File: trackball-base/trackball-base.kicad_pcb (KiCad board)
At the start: 2 copper layers, 110 x 140 mm, 159 parts, among them J201 TYPE-C-31-M-12, J202 CORTEX-DBG-10, Q101 2N7002, SW201 RESET, SW202 BOOT, SW401 D2FC-F-7N, SW402 D2FC-F-7N, SW403 D2FC-F-7N, U101 AP2112K-3.3TRG1, U102 APX809-29SAG-7, U103 XC6206P192MR, U104 TPS22918DBVR, U105 TPS22918DBVR, U106 TLV3011AIDBVR, U107 TLV3011AIDBVR, U201 E73-2G4M08S1C, U202 TPD2E1B06DRLR, U301 PMW3360DM-T2QU, U302 PMW3360DM-T2QU, U501 LTC4125EUFD, Y201 ABS07-32.768KHZ-9-T

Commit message: Q6 WaveC: J202-Pin2 closed (B-route + VSEN-via bypass + pad via); drc168 16unc/0err/0parity
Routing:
- net /mcu/Net-(J202-Pin_2): track 24.2 -> 43.3 mm, vias 2 -> 4
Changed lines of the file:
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@@
+	)
+	(via
+		(at 12.2 9.45)
+		(size 0.6)
+		(drill 0.3)
+		(layers "F.Cu" "B.Cu")
+		(net "/mcu/Net-(J202-Pin_2)")
+	)
+	(via
+		(at 9.95 19.7)
+		(size 0.6)
+		(drill 0.3)
+		(layers "F.Cu" "B.Cu")
+		(net "/mcu/Net-(J202-Pin_2)")
 	)
 	(via
@@
 		(drill 0.4)
 		(layers "F.Cu" "B.Cu")
+		(net "/mcu/Net-(J202-Pin_2)")
+	)
+	(segment
+		(start 13.8 9.45)
+		(end 13.8 16.85)
+		(width 0.25)
+		(layer "B.Cu")
+		(net "/mcu/Net-(J202-Pin_2)")
+	)
+	(segment
+		(start 9.95 19.46)
+		(end 9.95 20.5)
+		(width 0.25)
+		(layer "B.Cu")
+		(net "/mcu/Net-(J202-Pin_2)")
+	)
+	(segment
+		(start 9.95 20.5)
+		(end 13.8 20.5)
+		(width 0.25)
+		(layer "B.Cu")
+		(net "/mcu/Net-(J202-Pin_2)")
+	)
+	(segment
+		(start 13 18.15)
+		(end 13.8 18.15)
+		(width 0.25)
+		(layer "B.Cu")
+		(net "/mcu/Net-(J202-Pin_2)")
+	)
+	(segment
+		(start 13 16.85)
+		(end 13 18.15)
+		(width 0.25)
+		(layer "B.Cu")
 		(net "/mcu/Net-(J202-Pin_2)")
 	)
@@
 	)
 	(segment
+		(start 13.8 16.85)
+		(end 13 16.85)
+		(width 0.25)
+		(layer "B.Cu")
+		(net "/mcu/Net-(J202-Pin_2)")
+	)
+	(segment
 		(start 29.925 8.81)
 		(end 25.703 8.81)
 		(width 0.25)
 		(layer "B.Cu")
+		(net "/mcu/Net-(J202-Pin_2)")
+	)
+	(segment
+		(start 13.8 9.45)
+		(end 12.2 9.45)
+		(width 0.25)
+		(layer "B.Cu")
+		(net "/mcu/Net-(J202-Pin_2)")
+	)
+	(segment
+		(start 13.8 18.15)
+		(end 13.8 20.5)
+		(width 0.25)
+		(layer "B.Cu")

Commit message: Q6 WaveC complete: FTH ripped; drc177 16unc/0err/0parity; WaveD=15+WaveZ
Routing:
- net S2_MOT: track 83.5 -> 59.5 mm
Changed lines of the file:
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@@
-	)
-	(segment
-		(start 43.95 13.2)
-		(end 43.95 37.2)
-		(width 0.25)
-		(layer "F.Cu")
-		(net "S2_MOT")
 	)
 	(segment

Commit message: Oracle-1: TX_IMON closed via oracle corridor (W-dip + B@4.6 + F-rise + B-join); drc181 15unc/0err/0parity
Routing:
- net TX_IMON: track 14.5 -> 78.2 mm, vias 2 -> 7
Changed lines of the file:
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@@
+	)
+	(segment
+		(start 37 4.6)
+		(end 37 12.15)
+		(width 0.25)
+		(layer "F.Cu")
+		(net "TX_IMON")
+	)
+	(segment
+		(start 17.5 17.66)
+		(end 17.26 17.25)
+		(width 0.25)
+		(layer "F.Cu")
+		(net "TX_IMON")
 	)
 	(segment
@@
 		(end 53.062 17)
 		(width 0.3)
+		(layer "F.Cu")
+		(net "TX_IMON")
+	)
+	(segment
+		(start 20.61 7.37)
+		(end 20.61 4.6)
+		(width 0.25)
+		(layer "F.Cu")
+		(net "TX_IMON")
+	)
+	(segment
+		(start 37 12.15)
+		(end 39.55 14.7)
+		(width 0.25)
 		(layer "F.Cu")
 		(net "TX_IMON")
@@
 	)
 	(segment
+		(start 39.55 19.05)
+		(end 39.35 19.25)
+		(width 0.25)
+		(layer "F.Cu")
+		(net "TX_IMON")
+	)
+	(segment
 		(start 49.02 25)
 		(end 49.02 24)
@@
 	)
 	(segment
+		(start 17.5 17.66)
+		(end 20.09 17.66)
+		(width 0.25)
+		(layer "F.Cu")
+		(net "TX_IMON")
+	)
+	(segment
+		(start 18.9 8)
+		(end 20.16 8)
+		(width 0.25)
+		(layer "F.Cu")
+		(net "TX_IMON")
+	)
+	(segment
 		(start 52.935 17.025)
 		(end 53.062 17.025)
 		(width 0.3)
+		(layer "F.Cu")
+		(net "TX_IMON")
+	)
+	(segment
+		(start 20.16 8)
+		(end 20.61 7.37)
+		(width 0.25)
+		(layer "F.Cu")
+		(net "TX_IMON")
+	)
+	(segment
+		(start 20.09 17.66)
+		(end 20.09 18.9)
+		(width 0.25)
 		(layer "F.Cu")
 		(net "TX_IMON")
@@
 	)
 	(segment
+		(start 39.55 14.7)
+		(end 39.55 19.05)
+		(width 0.2)
+		(layer "F.Cu")
+		(net "TX_IMON")
+	)
+	(segment
 		(start 52.935 18)
 		(end 52.935 17.025)
@@
 		(width 0.3)
 		(layer "F.Cu")
+		(net "TX_IMON")
+	)
+	(segment
+		(start 17.26 17.25)
+		(end 17.26 16.12)
+		(width 0.25)
+		(layer "F.Cu")
+		(net "TX_IMON")
+	)
+	(via
+		(at 20.8 4.6)
+		(size 0.6)
+		(drill 0.3)
+		(layers "F.Cu" "B.Cu")
+		(net "TX_IMON")
+	)
+	(via
+		(at 17.26 16.12)
+		(size 0.6)
+		(drill 0.3)
+		(layers "F.Cu" "B.Cu")
+		(net "TX_IMON")
+	)
+	(via
+		(at 18.9 8)
+		(size 0.6)
+		(drill 0.3)
+		(layers "F.Cu" "B.Cu")
+		(net "TX_IMON")
+	)
+	(via
+		(at 37 4.6)
+		(size 0.6)
+		(drill 0.3)
+		(layers "F.Cu" "B.Cu")
 		(net "TX_IMON")
 	)
@@
 		(net "TX_IMON")
 	)
+	(via
+		(at 39.35 19.25)
+		(size 0.6)
+		(drill 0.3)
+		(layers "F.Cu" "B.Cu")
+		(net "TX_IMON")
+	)
 	(segment
 		(start 50.02 23.315)
@@
 	)
 	(segment
+		(start 16.8 10.16)
+		(end 19.23 8)
+		(width 0.25)
+		(layer "B.Cu")
+		(net "TX_IMON")
+	)
+	(segment
+		(start 19.23 8)
+		(end 18.9 8)
+		(width 0.25)
+		(layer "B.Cu")
+		(net "TX_IMON")
+	)
+	(segment
+		(start 44.1 24)
+		(end 49.02 24)
+		(width 0.25)
+		(layer "B.Cu")
+		(net "TX_IMON")
+	)
+	(segment
+		(start 39.35 19.25)
+		(end 44.1 24)
+		(width 0.25)
+		(layer "B.Cu")
+		(net "TX_IMON")
+	)
+	(segment
 		(start 52.562 20.535)
 		(end 52.788 20.535)
@@
 	)
 	(segment
+		(start 17.26 16.12)
+		(end 16.8 15.75)
+		(width 0.25)
+		(layer "B.Cu")
+		(net "TX_IMON")
+	)
+	(segment
 		(start 49.02 24)
 		(end 49.04 24)
@@
 	)
 	(segment
+		(start 20.8 4.6)
+		(end 37 4.6)
+		(width 0.25)
+		(layer "B.Cu")
+		(net "TX_IMON")
+	)
+	(segment
 		(start 50.02 21.51)
 		(end 51.02 21.51)
@@
 		(layer "B.Cu")
 		(net "TX_IMON")
+	)
+	(segment
+		(start 16.8 15.75)
+		(end 16.8 10.16)
+		(width 0.25)
+		(layer "B.Cu")
+		(net "TX_IMON")

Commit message: Oracle-2: MCU_RST-north closed via oracle corridor verbatim (F34.97/B36.0/F30.91); drc182 14unc/0err/0parity
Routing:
- net MCU_RST: track 225.3 -> 272.8 mm, vias 13 -> 15
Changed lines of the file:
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@@
+	)
+	(segment
+		(start 35.82 52.4)
+		(end 30.91 57.31)
+		(width 0.25)
+		(layer "F.Cu")
+		(net "MCU_RST")
 	)
 	(segment
@@
 	)
 	(segment
+		(start 30.91 70.03)
+		(end 33.49 72.6)
+		(width 0.25)
+		(layer "F.Cu")
+		(net "MCU_RST")
+	)
+	(segment
 		(start 31.2 30.24)
 		(end 31.2 29.6)
+		(width 0.25)
+		(layer "F.Cu")
+		(net "MCU_RST")
+	)
+	(segment
+		(start 30.91 57.31)
+		(end 30.91 70.03)
 		(width 0.25)
 		(layer "F.Cu")
@@
 	)
 	(segment
+		(start 33.49 72.6)
+		(end 34.47 72.6)
+		(width 0.25)
+		(layer "F.Cu")
+		(net "MCU_RST")
+	)
+	(segment
 		(start 62.82 70.75)
 		(end 62.82 67.24)
@@
 	)
 	(segment
+		(start 35.82 52.23)
+		(end 35.82 52.4)
+		(width 0.25)
+		(layer "F.Cu")
+		(net "MCU_RST")
+	)
+	(segment
 		(start 62.965 4.25)
 		(end 62.965 6.485)
@@
 	)
 	(segment
+		(start 34.97 29.6)
+		(end 34.97 40.61)
+		(width 0.25)
+		(layer "F.Cu")
+		(net "MCU_RST")
+	)
+	(segment
 		(start 32.725 29.6)
 		(end 34.2 28.925)
@@
 		(size 0.8)
 		(drill 0.4)
+		(layers "F.Cu" "B.Cu")
+		(net "MCU_RST")
+	)
+	(via
+		(at 35.82 52.23)
+		(size 0.6)
+		(drill 0.3)
 		(layers "F.Cu" "B.Cu")
 		(net "MCU_RST")
@@
 	)
 	(via
+		(at 34.97 40.61)
+		(size 0.6)
+		(drill 0.3)
+		(layers "F.Cu" "B.Cu")
+		(net "MCU_RST")
+	)
+	(via
 		(at 30.2 29.6)
 		(size 0.6)
@@
 	)
 	(segment
+		(start 36 41.64)
+		(end 36 52.05)
+		(width 0.25)
+		(layer "B.Cu")
+		(net "MCU_RST")
+	)
+	(segment
+		(start 34.97 40.61)
+		(end 36 41.64)
+		(width 0.25)
+		(layer "B.Cu")
+		(net "MCU_RST")
+	)
+	(segment
 		(start 37.43 20.69)
 		(end 36.93 20.69)
@@
 		(width 0.25)
 		(layer "B.Cu")
+		(net "MCU_RST")
+	)
+	(segment
+		(start 36 52.05)
+		(end 35.82 52.23)
+		(width 0.25)
+		(layer "B.Cu")

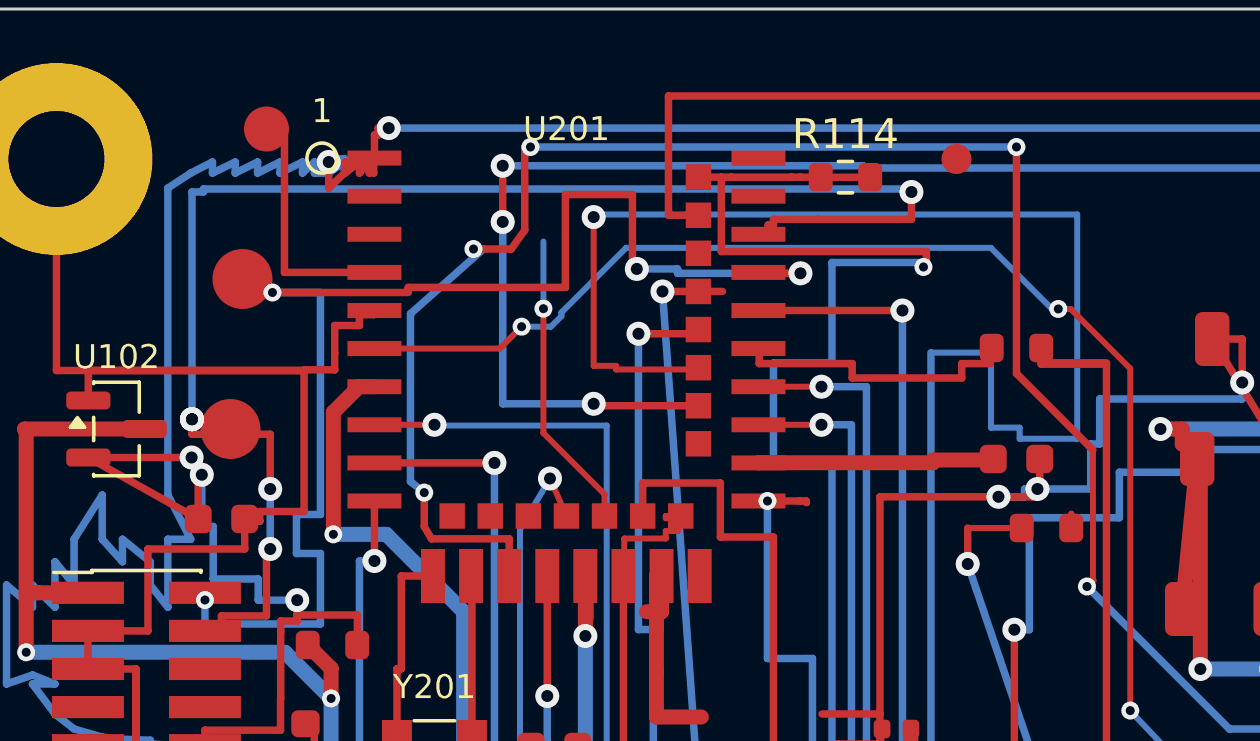
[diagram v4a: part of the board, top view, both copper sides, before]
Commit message: Q6 RIP CHECKPOINT drc185 22unc/0err/0parity: 65 ripped (S1_NCS-key/Pin_2/Pin_4/BTN3-w/P0.12-w/S2_MOSI-s); spines+anchors kept
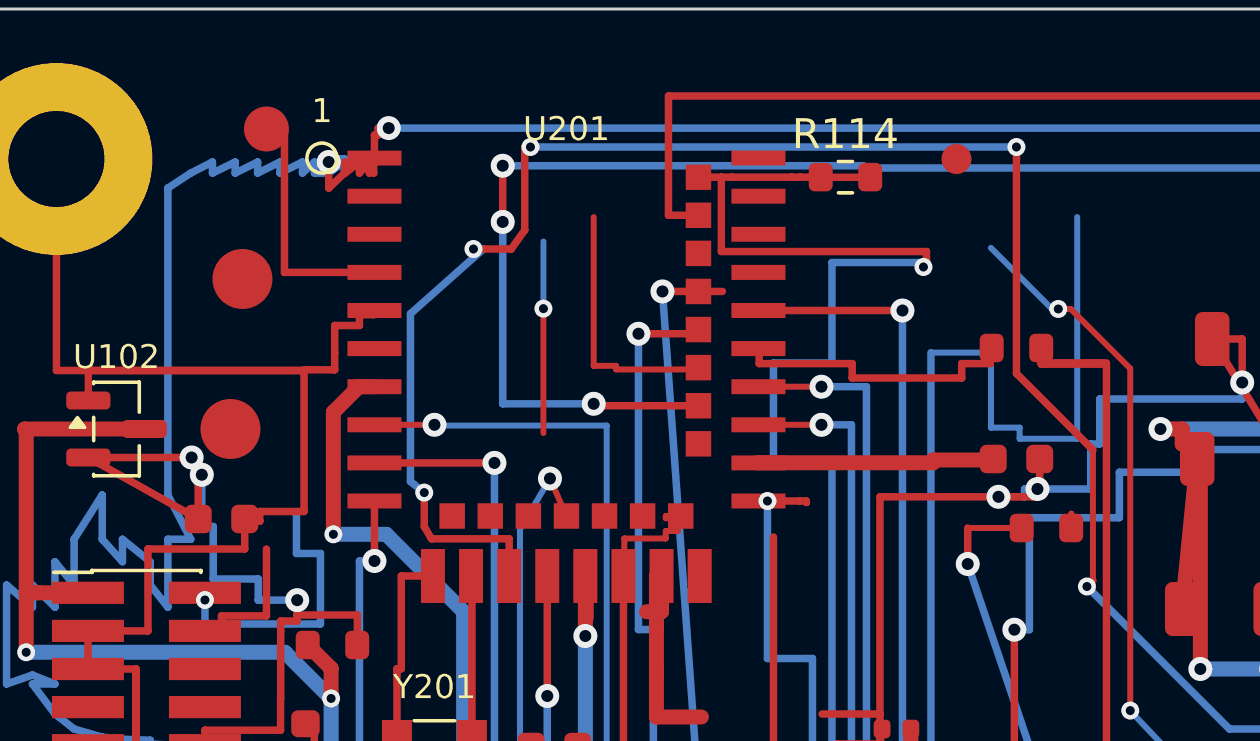
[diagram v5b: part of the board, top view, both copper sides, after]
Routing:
- net /mcu/Net-(J202-Pin_4): track 50.4 -> 4.78 mm, vias 5 -> 0
- net /mcu/Net-(J202-Pin_2): track 43.3 -> 9.34 mm, vias 4 -> 1
- net BTN3: track 136.2 -> 114.2 mm, vias 4 -> 3
- net S1_NCS: track 140.9 -> 124.6 mm, vias 4 -> 3
- net S2_MOSI: track 96.4 -> 89.1 mm
- net /mcu/Net-(U201-P0.12): track 10.6 -> 7.04 mm

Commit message: Q6 rip reverted drc186 14/0/0 (§7.10.8): triple-exclusion proof (S1_NCS/Pin_4/S2_MOT), R114 immovable, S2_MOT OPEN by proof
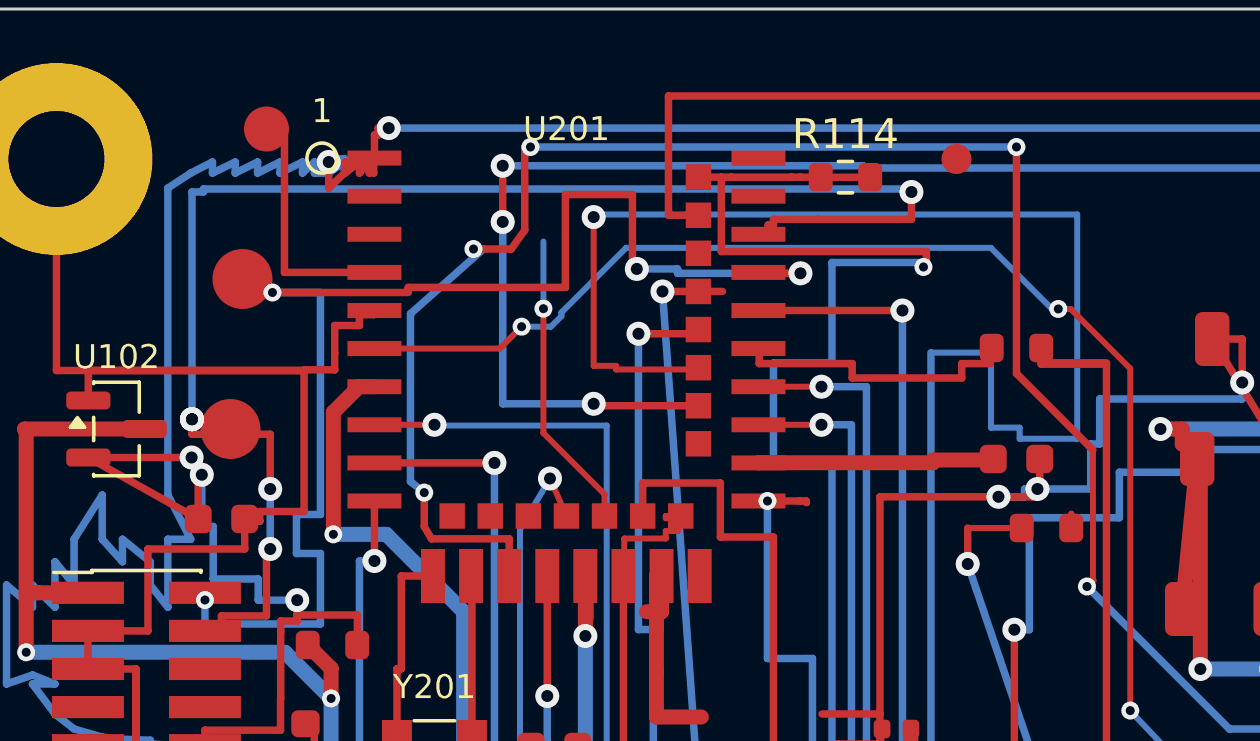
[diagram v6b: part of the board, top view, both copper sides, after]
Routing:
- net /mcu/Net-(J202-Pin_4): track 4.78 -> 50.4 mm, vias 0 -> 5
- net /mcu/Net-(J202-Pin_2): track 9.34 -> 43.3 mm, vias 1 -> 4
- net BTN3: track 114.2 -> 136.2 mm, vias 3 -> 4
- net S1_NCS: track 124.6 -> 140.9 mm, vias 3 -> 4
- net S2_MOSI: track 89.1 -> 96.4 mm
- net /mcu/Net-(U201-P0.12): track 7.04 -> 10.6 mm

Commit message: 4L stackup live + Wave-1 net-zero drc193 (§7.10.13: VIN/S2_MOT/P0.12 4L-dead, survey procedure)
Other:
- copper layers 2 -> 4
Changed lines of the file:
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@@
 	(layers
 		(0 "F.Cu" signal)
+		(4 "In1.Cu" signal)
+		(6 "In2.Cu" signal)
 		(2 "B.Cu" signal)
 		(9 "F.Adhes" user "F.Adhesive")

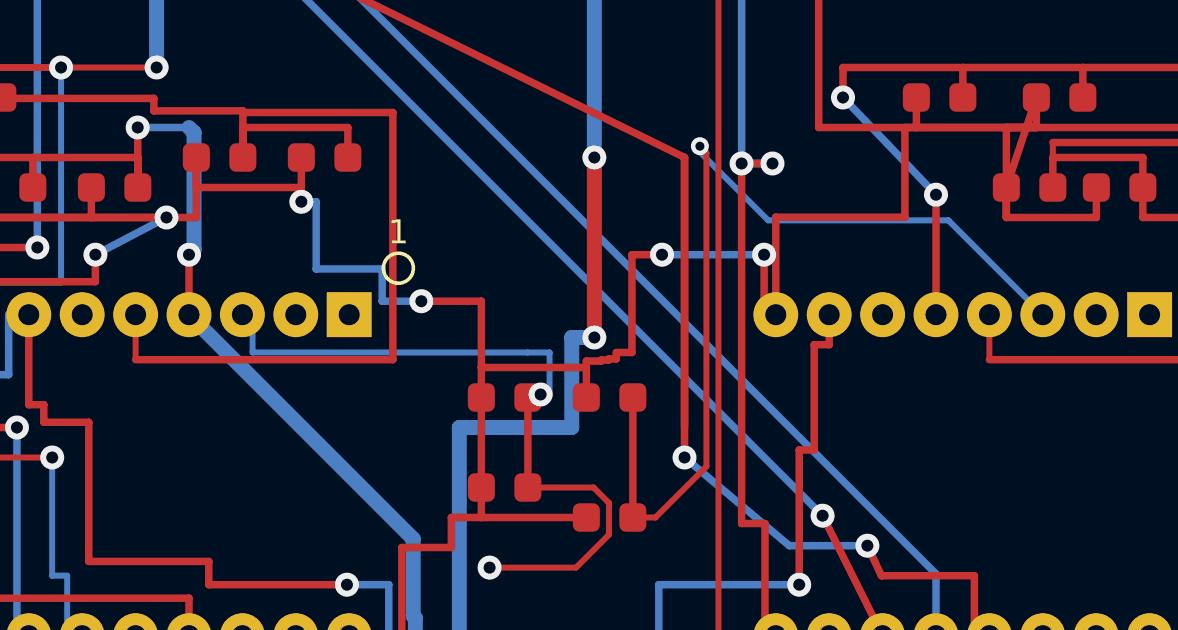
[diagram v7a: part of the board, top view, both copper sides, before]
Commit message: Wave-3 VSEN CLOSED drc198 13/0/0 (§7.10.15: In2 @63.50, first 4L close)
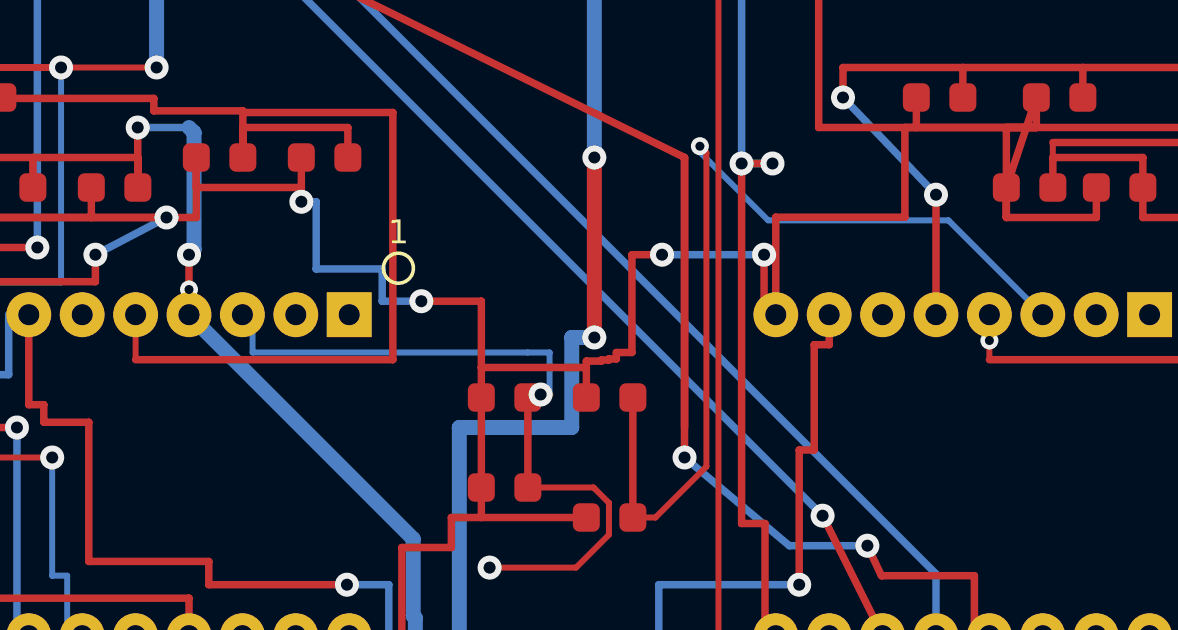
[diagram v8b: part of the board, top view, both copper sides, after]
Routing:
- net VSEN_1V9: track 222.8 -> 255.0 mm, vias 6 -> 8
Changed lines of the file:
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@@
+	)
+	(via
+		(at 68.66 67.1)
+		(size 0.6)
+		(drill 0.3)
+		(layers "F.Cu" "B.Cu")
+		(net "VSEN_1V9")
+	)
+	(via
+		(at 41.98 65.4)
+		(size 0.6)
+		(drill 0.3)
+		(layers "F.Cu" "B.Cu")
+		(net "VSEN_1V9")
 	)
 	(via
@@
 		(net "VSEN_1V9")
 	)
+	(segment
+		(start 41.98 63.5)
+		(end 68.66 63.5)
+		(width 0.25)
+		(layer "In2.Cu")
+		(net "VSEN_1V9")
+	)
+	(segment
+		(start 41.98 65.4)
+		(end 41.98 63.5)
+		(width 0.25)
+		(layer "In2.Cu")
+		(net "VSEN_1V9")
+	)
+	(segment
+		(start 68.66 63.5)
+		(end 68.66 67.1)
+		(width 0.25)
+		(layer "In2.Cu")
+		(net "VSEN_1V9")
+	)
